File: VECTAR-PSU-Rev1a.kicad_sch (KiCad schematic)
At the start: 52 parts, among them J1 Conn_01x02_Pin, J2 Conn_01x02_Pin, J3 Conn_01x02_Pin, J4 Conn_01x02_Pin, J78 Conn_01x02_Pin, Q78 2N7002, Q8 2N7002, SW78 SW_SPST, SW79 SW_SPST, U15 SY8253ADC

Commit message: Rev1b Design of PSU
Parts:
- removed J4: Conn_01x02_Pin, symbol Connector:Conn_01x02_Pin
- added J5: Conn_01x06_Socket, symbol Connector:Conn_01x06_Socket
- F1: renamed from F78; footprint (none) -> ul_3-140-172:FUSE_3-140-172_SCH
- J2, J3: footprint Connector_AMASS:AMASS_XT60-F_1x02_P7.20mm_Vertical -> Connector_AMASS:AMASS_XT60PW-M_1x02_P7.20mm_Horizontal
- renumbered C90 to C1, C89 to C2, C88 to C3, C87 to C4, C94 to C5, C93 to C6, C92 to C7, C91 to C8, C86 to C9, CR78 to CR1, D80 to CR2, D79 to D1, D81 to D2, J78 to J1, J1 to J4, Q78 to Q1, R81 to R1, R80 to R2, R84 to R3, R85 to R4, R86 to R5, R87 to R6, SW78 to SW1, SW79 to SW2, TP4 to TP1
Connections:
- net +3V3 is gone; now on net +5V: CR2.2 (A), R52.2
- net +12V: no longer C64.2, C67.2, TP1.1, U15.5 (VIN)
- net +5V: now also J5.1 (Pin_1), J5.2 (Pin_2)
- net +BATT: now also C1.1, C2.1, C3.1, PS78.1 (VIN(+)), SW1.1 (A)
- net GND: now also J5.3 (Pin_3), J5.4 (Pin_4), J5.5 (Pin_5), J5.6 (Pin_6)
- new net: C64.2, C67.2, TP1.1, U15.5 (VIN)
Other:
- moved on the sheet: TP1

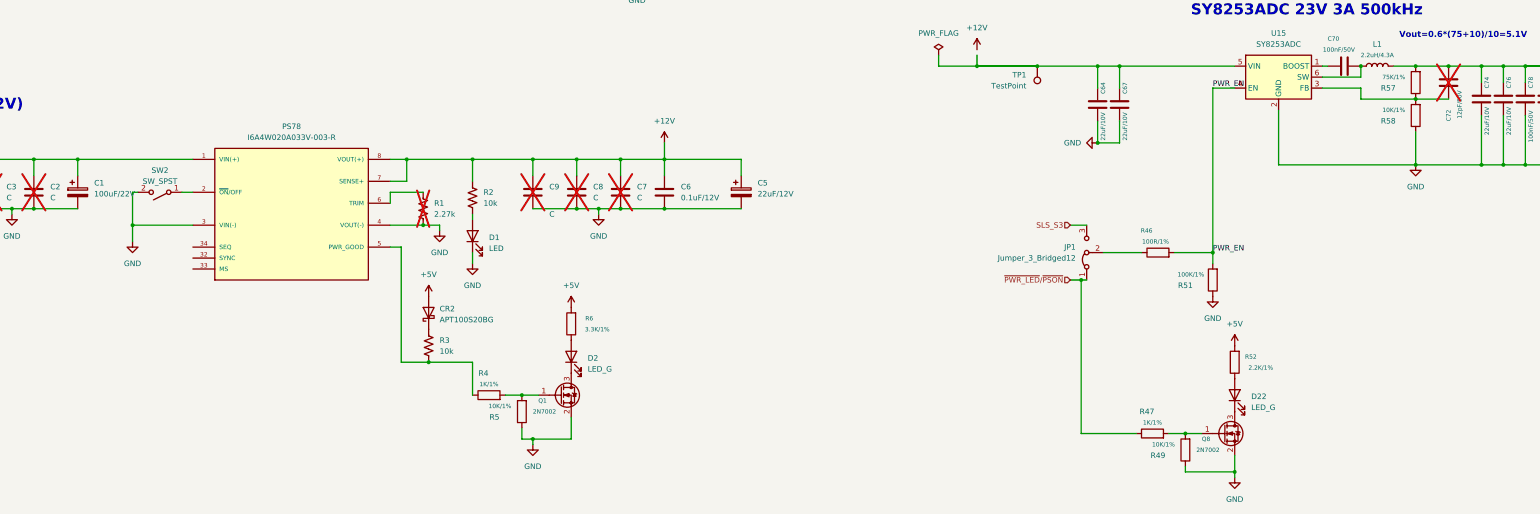
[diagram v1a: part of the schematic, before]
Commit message: Cleaned up libraries and added some testpoints. Need to finalize PG circuit and testpoint locations
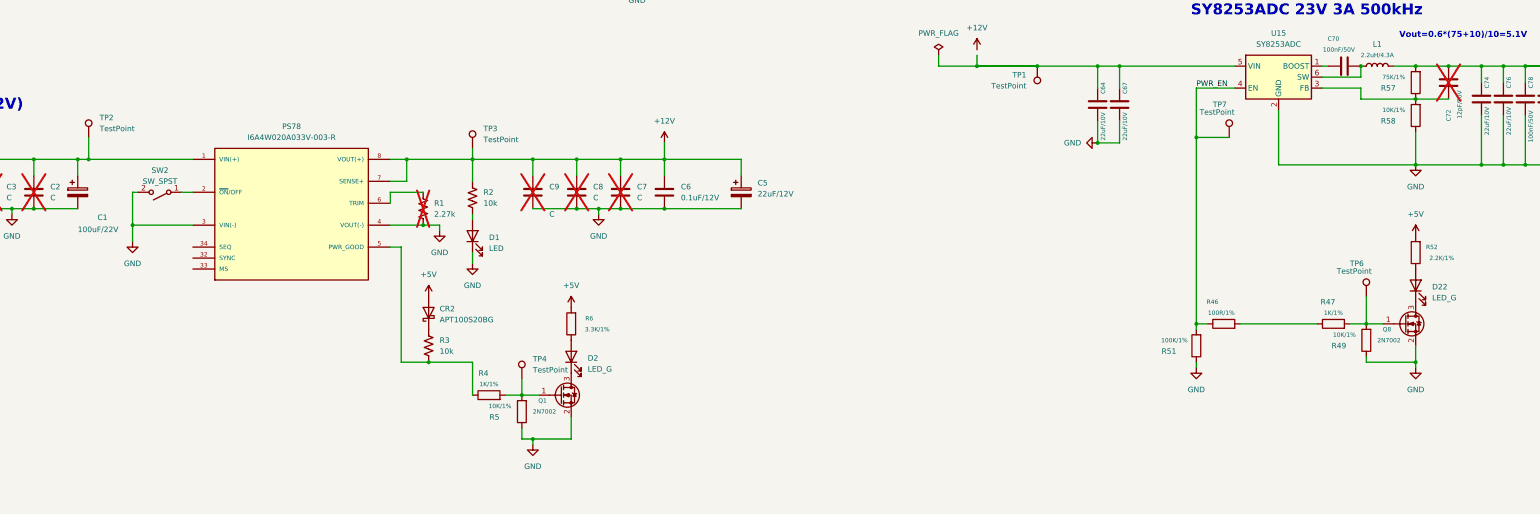
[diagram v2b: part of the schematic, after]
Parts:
- removed JP1: Jumper_3_Bridged12, A_HDJ_Library:PinHeader_1x03_P2.54mm_Vertical, symbol Jumper:Jumper_3_Bridged12
- added TP2, TP3, TP4, TP6, TP7: TestPoint, symbol Connector:TestPoint
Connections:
- net +12V: now also TP3.1
- net +BATT: now also TP2.1
- net PWR_EN: now also R46.1, TP7.1; no longer R46.2
- net at Q8.1 (G), R47.2, R49.2: now also TP6.1
- net at Q1.1 (G), R4.2, R5.2: now also TP4.1
- net ~{PWR_LED}/~{PSON}: no longer names the net of R47.1
- net ~{PWR_LED}/~{PSON}: now also R46.2
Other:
- moved on the sheet: D22, Q8, R46, R47, R49, R51, R52

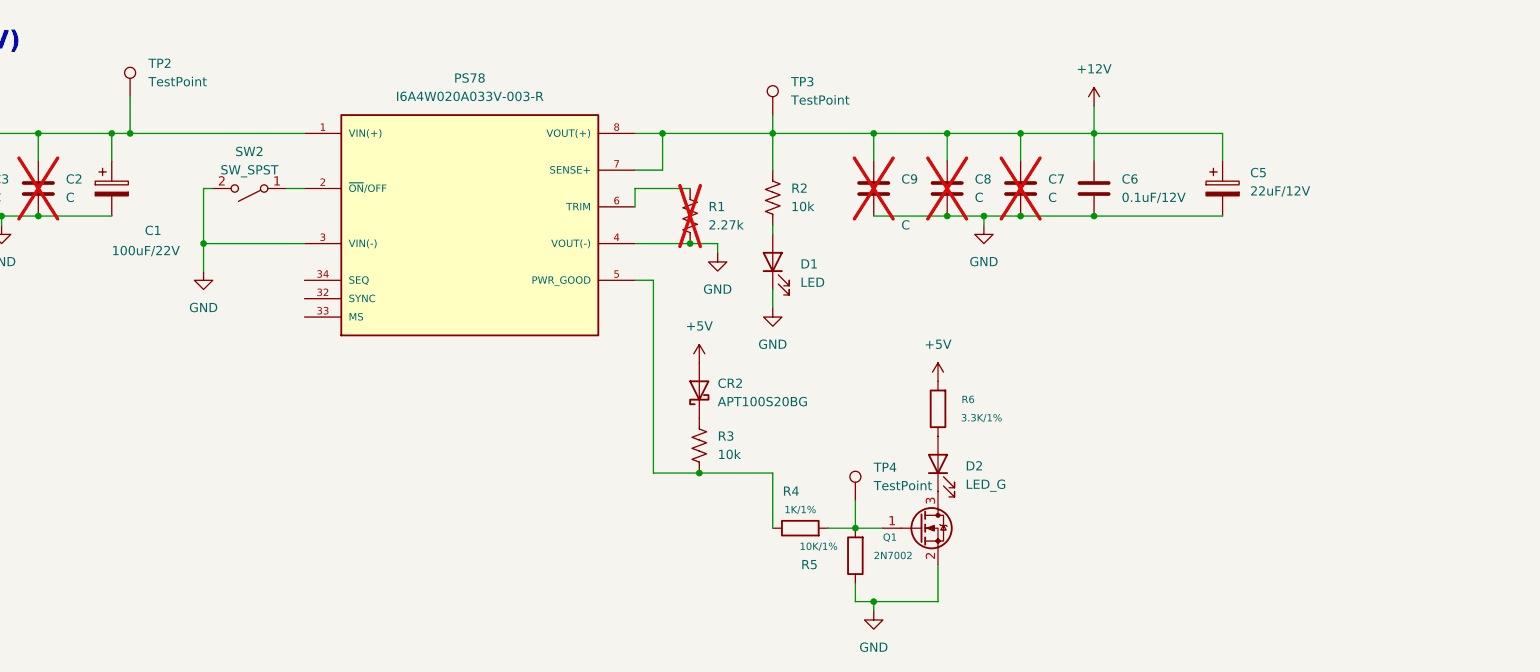
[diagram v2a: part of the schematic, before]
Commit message: updated PG circuit on 12V converter
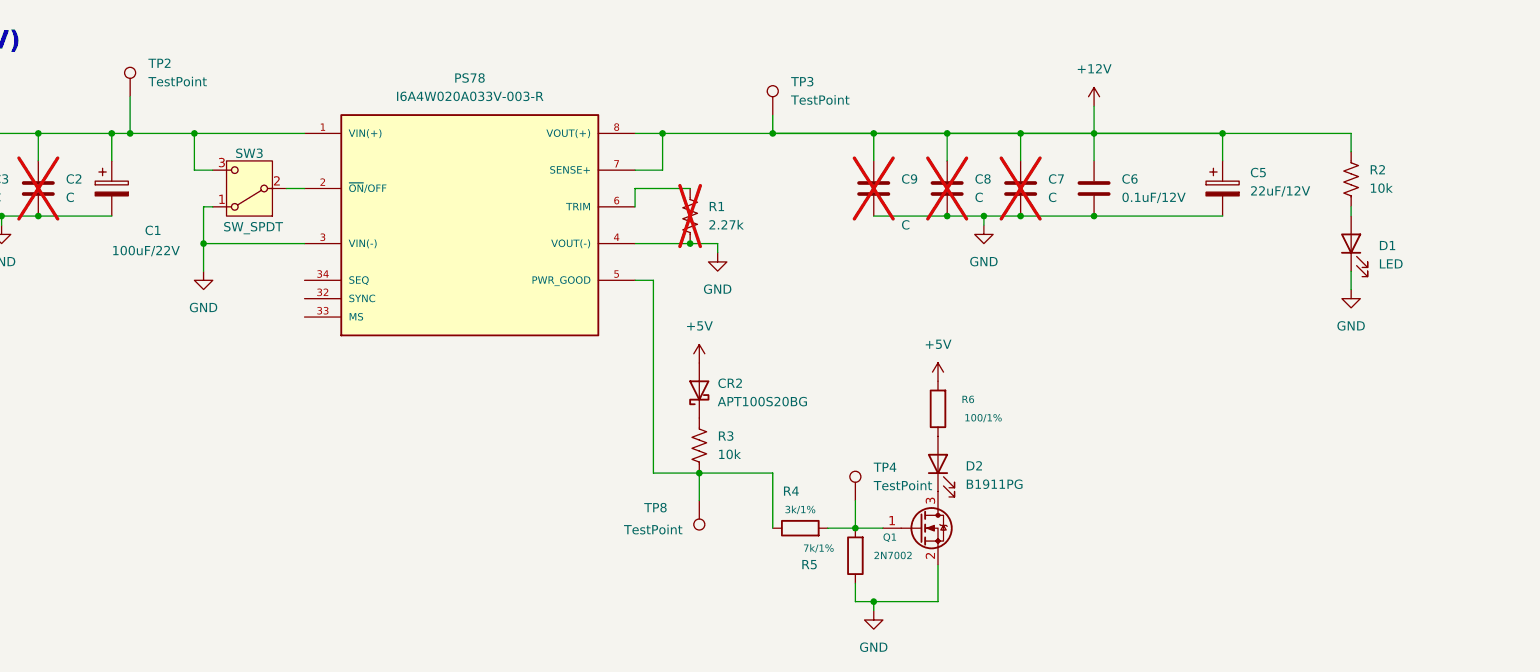
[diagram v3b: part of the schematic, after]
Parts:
- removed SW2: SW_SPST, Button_Switch_SMD:SW_Tactile_SPST_NO_Straight_CK_PTS636Sx25SMTRLFS, symbol Switch:SW_SPST
- added SW3: SW_SPDT, symbol Switch:SW_SPDT
- added TP8: TestPoint, symbol Connector:TestPoint
- D2: value LED_G -> B1911PG
- R4: value 1K/1% -> 3k/1%
- R5: value 10K/1% -> 7k/1%
- R6: value 3.3K/1% -> 100/1%
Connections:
- net +BATT: now also SW3.3 (C)
- net GND: now also SW3.1 (A)
- net at PS78.5 (PWR_GOOD), R3.2, R4.1: now also TP8.1
- net at PS78.2 (~{ON}/OFF): now also SW3.2 (B)
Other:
- moved on the sheet: D1, R2
